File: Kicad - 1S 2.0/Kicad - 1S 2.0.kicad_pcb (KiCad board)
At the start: 2 copper layers, 40 x 40 mm, 25 parts, among them J1 HRO_TYPE_C_31_M_12, J2 Conn_01x02, SW1 SW_SPDT, U1 BQ24074RGT, U2 TLV62569DBV

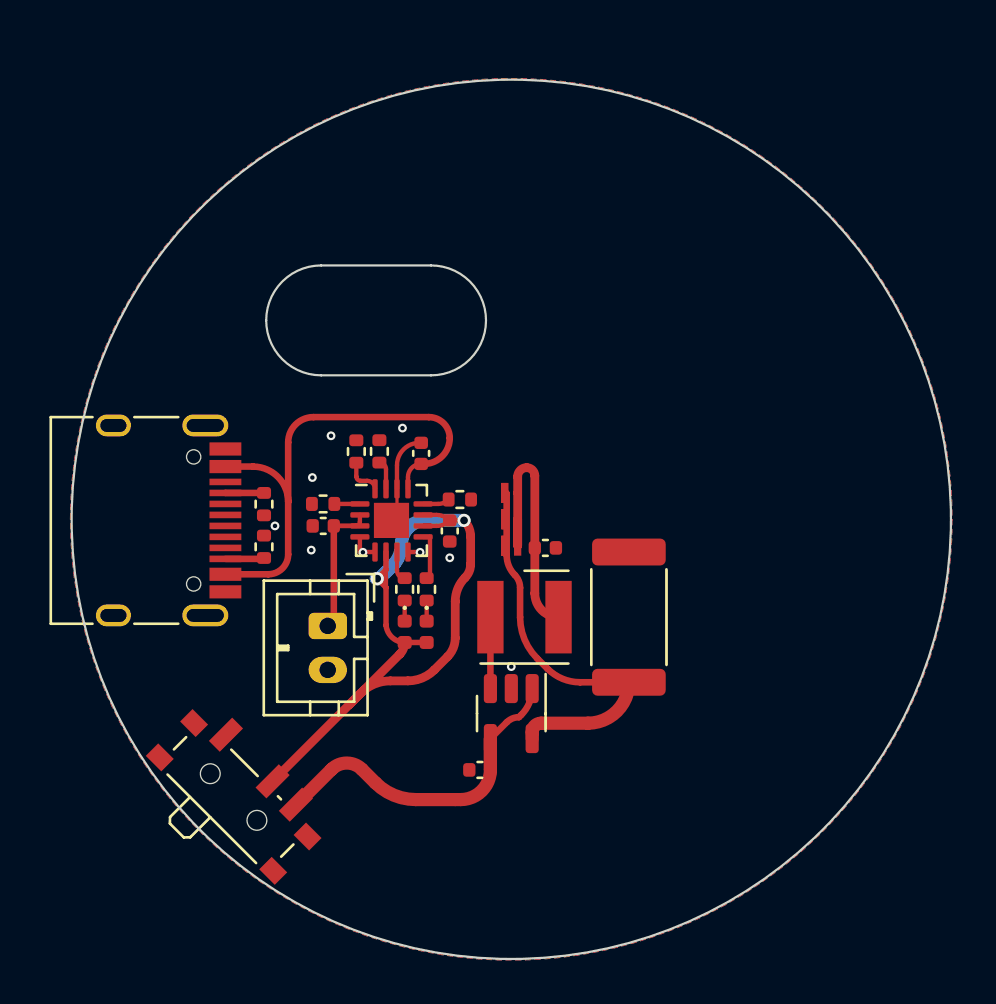
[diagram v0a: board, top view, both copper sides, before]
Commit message: changed LEDs over to a standard format to make the board cheaper
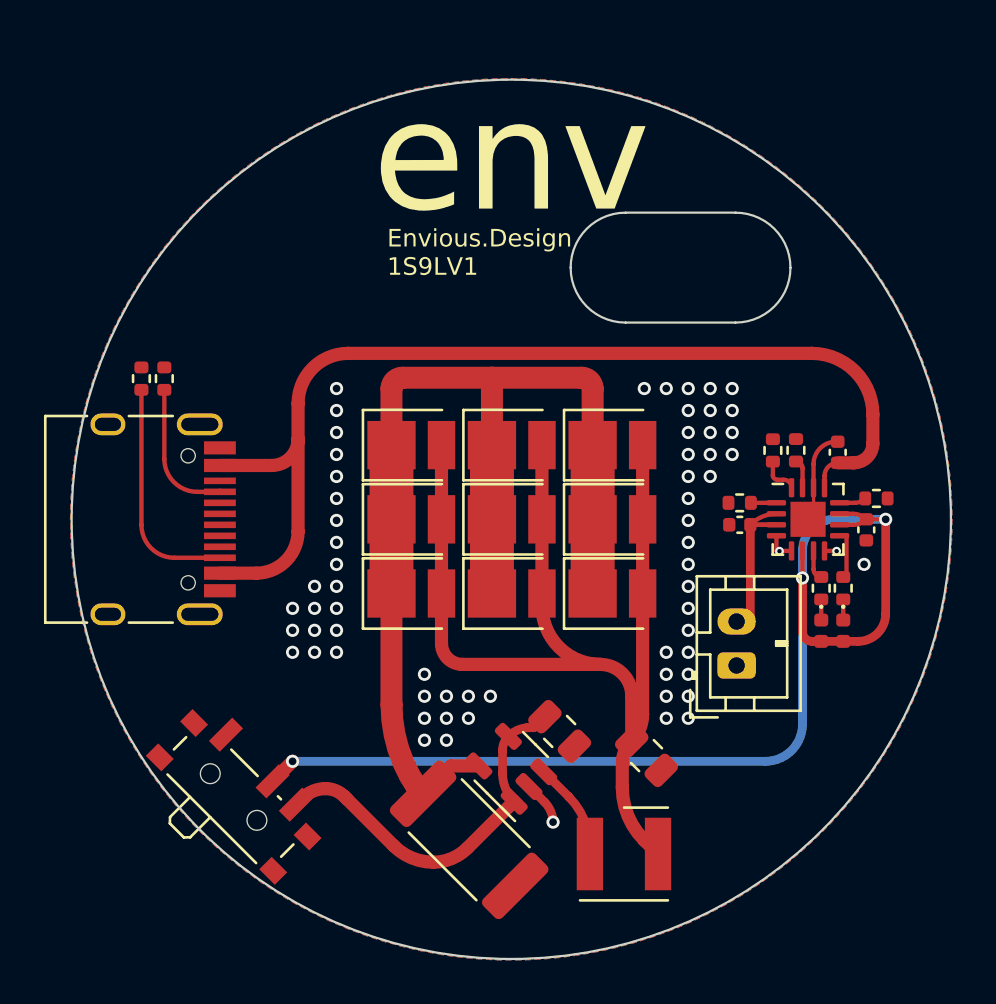
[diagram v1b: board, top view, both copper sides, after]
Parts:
- added MainLED4: GW JTLMS1.EM-GWH4-XX51-1, LED_SMD:LED_PLCC_2835, F.Cu at (43.5, 35.0)
- added MainLED5: GW JTLMS1.EM-GWH4-XX51-1, LED_SMD:LED_PLCC_2835, F.Cu at (43.5, 31.6)
- added MainLED6: GW JTLMS1.EM-GWH4-XX51-1, LED_SMD:LED_PLCC_2835, F.Cu at (39.0, 35.0)
- added MainLED7: GW JTLMS1.EM-GWH4-XX51-1, LED_SMD:LED_PLCC_2835, F.Cu at (39.0, 31.6)
- added MainLED8: GW JTLMS1.EM-GWH4-XX51-1, LED_SMD:LED_PLCC_2835, F.Cu at (39.0, 38.3)
- added MainLED9: GW JTLMS1.EM-GWH4-XX51-1, LED_SMD:LED_PLCC_2835, F.Cu at (43.5, 38.3)
- C4, C5: value 0402 4.7uF -> 0805 4.7uF; footprint Capacitor_SMD:C_0402_1005Metric -> Capacitor_SMD:C_0805_2012Metric
- MainLED1, MainLED2, MainLED3: value GW VJLPE1 -> GW JTLMS1.EM-GWH4-XX51-1; footprint VJLPE1:VJLPE1 -> LED_SMD:LED_PLCC_2835
- R9: value 400mΩ 2512 -> 500mΩ 2512
- moved C1 19.0 mm to (55.1, 35.4)
- moved R3 19.0 mm to (50.9, 31.8)
- moved R6 19.0 mm to (49.3, 34.2)
- moved U1 19.0 mm to (52.5, 35.0)
- moved C2 19.0 mm to (49.3, 35.2)
- moved D1 19.0 mm to (53.0, 40.0)
- moved D2 19.0 mm to (54.0, 40.0)
- moved R1 19.0 mm to (51.9, 31.8)
- moved R2 19.0 mm to (55.6, 34.0)
- moved R4 19.0 mm to (54.0, 38.1)
- moved R5 19.0 mm to (53.0, 38.1)
- moved C3 19.0 mm to (53.8, 31.9)
- moved J2 18.7 mm to (49.2, 41.6), turned to 90 degrees
- moved R9 12.5 mm to (37.0, 49.5), turned to -45 degrees
- moved L1 11.7 mm to (44.1, 50.2)
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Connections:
- C2 pad 1: Net-(J2-Pin_1) -> Net-(J2-Pin_2)
- J2 pad 1: Net-(J2-Pin_1) -> GND
- J2 pad 2: GND -> Net-(J2-Pin_2)
- U1 pad 2: Net-(J2-Pin_1) -> Net-(J2-Pin_2)
- U1 pad 3: Net-(J2-Pin_1) -> Net-(J2-Pin_2)
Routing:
- net Net-(MainLED1-A): track 12.5 -> 51.7 mm
- net Net-(MainLED1-K): track 18.4 -> 50.6 mm
- net VBUS: track 24.0 -> 48.4 mm
- net OUT: track 36.8 -> 53.9 mm, vias 2 -> 3
- net Net-(J2-Pin_2): track 0.00 -> 13.6 mm
- net Net-(J1-CC2): track 1.77 -> 10.5 mm
- net Net-(J2-Pin_1): track 7.48 -> 0.00 mm
- net Net-(J1-CC1): track 1.76 -> 6.47 mm
- net GND: track 6.35 -> 8.39 mm, vias 9 -> 65
- net Net-(U2-SW): track 3.25 -> 4.45 mm
- net SWITCHED_OUT: track 16.7 -> 17.5 mm
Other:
- outline, holes or cut-outs redrawn
- board text added: "Envious.Design 1S9LV1"
- board text removed: "Env_LedTorch02"
- board text removed: "Envious.Design"
